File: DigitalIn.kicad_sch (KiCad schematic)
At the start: 5 parts, among them U7 LTV-247

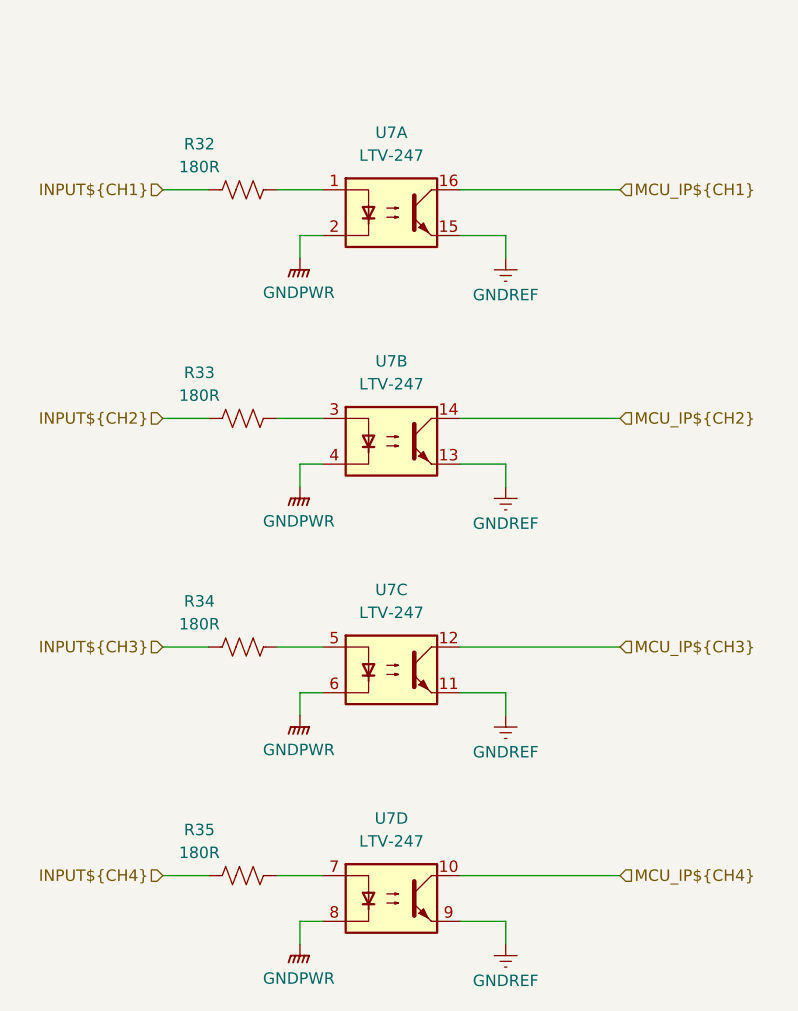
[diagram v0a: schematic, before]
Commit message: Changes to input after testing with some optical sensors
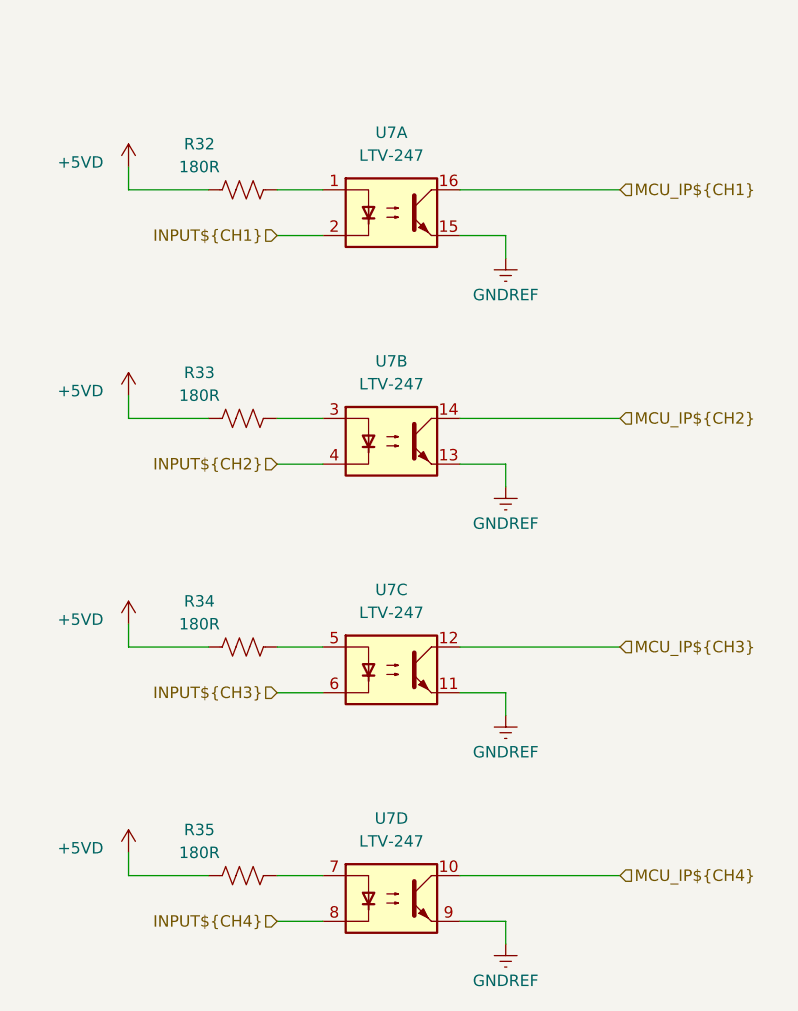
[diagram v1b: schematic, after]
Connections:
- net INPUT${CH1}: now also U7.2; no longer R32.1
- net INPUT${CH2}: now also U7.4; no longer R33.1
- net INPUT${CH3}: now also U7.6; no longer R34.1
- net INPUT${CH4}: now also U7.8; no longer R35.1
- removed net GNDPWR: U7.2, U7.4, U7.6, U7.8
- new net +5VD: R32.1, R33.1, R34.1, R35.1

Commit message: Added high speed encoder input circuitry. General tidy and updates to readme
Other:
- note added: "NPN Inputs"
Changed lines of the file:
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@@
 	(generator_version "9.0")
 	(paper "A4")
+	(text "NPN Inputs"
+		(exclude_from_sim no)
+		(at 149.606 35.814 0)
+		(effects
+			(font
+				(size 1.27 1.27)
+			)
+		)
+	)
 	(wire
 		(pts
@@
 			(project "Remora Nucleo F446ZE Hat"
 				(path "/5473abc6-7b93-43cc-a401-f691c4d7d7cf/181d5939-8311-41b3-8216-f7233e3a75eb/1fe6751c-d44f-4f1b-8c0c-fbb5540720e0"
-					(reference "#PWR0219")
+					(reference "#PWR0225")
 					(unit 1)
 				)
@@
 			(project ""
 				(path "/5473abc6-7b93-43cc-a401-f691c4d7d7cf/181d5939-8311-41b3-8216-f7233e3a75eb/1fe6751c-d44f-4f1b-8c0c-fbb5540720e0"
-					(reference "U20")
+					(reference "U16")
 					(unit 4)
 				)
@@
 			(project "Remora Nucleo F446ZE Hat"
 				(path "/5473abc6-7b93-43cc-a401-f691c4d7d7cf/181d5939-8311-41b3-8216-f7233e3a75eb/1fe6751c-d44f-4f1b-8c0c-fbb5540720e0"
-					(reference "#PWR0217")
+					(reference "#PWR0223")
 					(unit 1)
 				)
@@
 			(project "Remora Nucleo F446ZE Hat"
 				(path "/5473abc6-7b93-43cc-a401-f691c4d7d7cf/181d5939-8311-41b3-8216-f7233e3a75eb/1fe6751c-d44f-4f1b-8c0c-fbb5540720e0"
-					(reference "#PWR0214")
+					(reference "#PWR0220")
 					(unit 1)
 				)
@@
 			(project "Remora Nucleo F446ZE Hat"
 				(path "/5473abc6-7b93-43cc-a401-f691c4d7d7cf/181d5939-8311-41b3-8216-f7233e3a75eb/1fe6751c-d44f-4f1b-8c0c-fbb5540720e0"
-					(reference "R88")
+					(reference "R95")
 					(unit 1)
 				)
@@
 			(project ""
 				(path "/5473abc6-7b93-43cc-a401-f691c4d7d7cf/181d5939-8311-41b3-8216-f7233e3a75eb/1fe6751c-d44f-4f1b-8c0c-fbb5540720e0"
-					(reference "U20")
+					(reference "U17")
 					(unit 2)
 				)
@@
 			(project ""
 				(path "/5473abc6-7b93-43cc-a401-f691c4d7d7cf/181d5939-8311-41b3-8216-f7233e3a75eb/1fe6751c-d44f-4f1b-8c0c-fbb5540720e0"
-					(reference "U20")
+					(reference "U17")
 					(unit 3)
 				)
@@
 			(project "Remora Nucleo F446ZE Hat"
 				(path "/5473abc6-7b93-43cc-a401-f691c4d7d7cf/181d5939-8311-41b3-8216-f7233e3a75eb/1fe6751c-d44f-4f1b-8c0c-fbb5540720e0"
-					(reference "#PWR0218")
+					(reference "#PWR0224")
 					(unit 1)
 				)
@@
 			(project "Remora Nucleo F446ZE Hat"
 				(path "/5473abc6-7b93-43cc-a401-f691c4d7d7cf/181d5939-8311-41b3-8216-f7233e3a75eb/1fe6751c-d44f-4f1b-8c0c-fbb5540720e0"
-					(reference "R89")
+					(reference "R96")
 					(unit 1)
 				)
@@
 			(project "Remora Nucleo F446ZE Hat"
 				(path "/5473abc6-7b93-43cc-a401-f691c4d7d7cf/181d5939-8311-41b3-8216-f7233e3a75eb/1fe6751c-d44f-4f1b-8c0c-fbb5540720e0"
-					(reference "#PWR0216")
+					(reference "#PWR0222")
 					(unit 1)
 				)
@@
 			(project "Remora Nucleo F446ZE Hat"
 				(path "/5473abc6-7b93-43cc-a401-f691c4d7d7cf/181d5939-8311-41b3-8216-f7233e3a75eb/1fe6751c-d44f-4f1b-8c0c-fbb5540720e0"
-					(reference "#PWR0221")
+					(reference "#PWR0227")
 					(unit 1)
 				)
@@
 			(project ""
 				(path "/5473abc6-7b93-43cc-a401-f691c4d7d7cf/181d5939-8311-41b3-8216-f7233e3a75eb/1fe6751c-d44f-4f1b-8c0c-fbb5540720e0"
-					(reference "U20")
+					(reference "U19")
 					(unit 1)
 				)
@@
 			(project "Remora Nucleo F446ZE Hat"
 				(path "/5473abc6-7b93-43cc-a401-f691c4d7d7cf/181d5939-8311-41b3-8216-f7233e3a75eb/1fe6751c-d44f-4f1b-8c0c-fbb5540720e0"
-					(reference "#PWR0215")
+					(reference "#PWR0221")
 					(unit 1)
 				)
@@
 			(project "Remora Nucleo F446ZE Hat"
 				(path "/5473abc6-7b93-43cc-a401-f691c4d7d7cf/181d5939-8311-41b3-8216-f7233e3a75eb/1fe6751c-d44f-4f1b-8c0c-fbb5540720e0"
-					(reference "#PWR0220")
+					(reference "#PWR0226")
 					(unit 1)
 				)
@@
 			(project "Remora Nucleo F446ZE Hat"
 				(path "/5473abc6-7b93-43cc-a401-f691c4d7d7cf/181d5939-8311-41b3-8216-f7233e3a75eb/1fe6751c-d44f-4f1b-8c0c-fbb5540720e0"
-					(reference "R90")
+					(reference "R97")
 					(unit 1)
 				)
@@
 			(project "Remora Nucleo F446ZE Hat"
 				(path "/5473abc6-7b93-43cc-a401-f691c4d7d7cf/181d5939-8311-41b3-8216-f7233e3a75eb/1fe6751c-d44f-4f1b-8c0c-fbb5540720e0"
-					(reference "R91")
-					(unit 1)
-				)
+					(reference "R98")
+					(unit 1)
+				)

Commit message: Layout for stepper drivers and digital inputs
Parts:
- renumbered U7 to U
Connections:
- net GNDREF: now also U.15, U.15, U.15; no longer U.11, U.13, U.9
- net INPUT${CH2}: now also U.2; no longer U.4
- net INPUT${CH3}: now also U.2; no longer U.6
- net INPUT${CH4}: now also U.2; no longer U.8
- net MCU_IP${CH2}: now also U.16; no longer U.14
- net MCU_IP${CH3}: now also U.16; no longer U.12
- net MCU_IP${CH4}: now also U.16; no longer U.10
- net at R35.2: now also U.1; no longer U.7
- net at R33.2: now also U.1; no longer U.3
- net at R34.2: now also U.1; no longer U.5
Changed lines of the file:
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@@
 		(instances
 			(project "Remora Nucleo F446ZE Hat"
-				(path "/5473abc6-7b93-43cc-a401-f691c4d7d7cf/181d5939-8311-41b3-8216-f7233e3a75eb/1fe6751c-d44f-4f1b-8c0c-fbb5540720e0"
-					(reference "#PWR0225")
+				(path "/5473abc6-7b93-43cc-a401-f691c4d7d7cf/181d5939-8311-41b3-8216-f7233e3a75eb/0efd5135-f8b7-4cd1-8e93-f14156388778"
+					(reference "#PWR0228")
 					(unit 1)
 				)
@@
 		(lib_id "Isolator:LTV-247")
 		(at 149.86 132.08 0)
-		(unit 4)
+		(unit 1)
 		(exclude_from_sim no)
 		(in_bom yes)
@@
 		(dnp no)
 		(fields_autoplaced yes)
-		(property "Reference" "U7"
+		(property "Reference" "U"
 			(at 149.86 123.19 0)
 			(effects
@@
 		)
 		(instances
-			(project ""
-				(path "/5473abc6-7b93-43cc-a401-f691c4d7d7cf/181d5939-8311-41b3-8216-f7233e3a75eb/1fe6751c-d44f-4f1b-8c0c-fbb5540720e0"
+			(project "Remora Nucleo F446ZE Hat"
+				(path "/5473abc6-7b93-43cc-a401-f691c4d7d7cf/181d5939-8311-41b3-8216-f7233e3a75eb/0efd5135-f8b7-4cd1-8e93-f14156388778"
 					(reference "U16")
 					(unit 4)
 				)
-				(path "/5473abc6-7b93-43cc-a401-f691c4d7d7cf/181d5939-8311-41b3-8216-f7233e3a75eb/38a9b34d-220a-4331-8671-09e3a6b76818"
-					(reference "U10")
-					(unit 4)
-				)
-				(path "/5473abc6-7b93-43cc-a401-f691c4d7d7cf/181d5939-8311-41b3-8216-f7233e3a75eb/3ddea5d6-e83a-4299-ab19-77514b1abca5"
-					(reference "U9")
-					(unit 4)
-				)
-				(path "/5473abc6-7b93-43cc-a401-f691c4d7d7cf/181d5939-8311-41b3-8216-f7233e3a75eb/adf08f85-0659-4d18-9c0c-1da5c9849bec"
-					(reference "U7")
-					(unit 4)
-				)
 			)
 		)
@@
 		(instances
 			(project "Remora Nucleo F446ZE Hat"
-				(path "/5473abc6-7b93-43cc-a401-f691c4d7d7cf/181d5939-8311-41b3-8216-f7233e3a75eb/1fe6751c-d44f-4f1b-8c0c-fbb5540720e0"
-					(reference "#PWR0223")
+				(path "/5473abc6-7b93-43cc-a401-f691c4d7d7cf/181d5939-8311-41b3-8216-f7233e3a75eb/0efd5135-f8b7-4cd1-8e93-f14156388778"
+					(reference "#PWR0226")
 					(unit 1)
 				)
@@
 		(instances
 			(project "Remora Nucleo F446ZE Hat"
-				(path "/5473abc6-7b93-43cc-a401-f691c4d7d7cf/181d5939-8311-41b3-8216-f7233e3a75eb/1fe6751c-d44f-4f1b-8c0c-fbb5540720e0"
-					(reference "#PWR0220")
+				(path "/5473abc6-7b93-43cc-a401-f691c4d7d7cf/181d5939-8311-41b3-8216-f7233e3a75eb/0efd5135-f8b7-4cd1-8e93-f14156388778"
+					(reference "#PWR0223")
 					(unit 1)
 				)
@@
 		(instances
 			(project "Remora Nucleo F446ZE Hat"
-				(path "/5473abc6-7b93-43cc-a401-f691c4d7d7cf/181d5939-8311-41b3-8216-f7233e3a75eb/1fe6751c-d44f-4f1b-8c0c-fbb5540720e0"
+				(path "/5473abc6-7b93-43cc-a401-f691c4d7d7cf/181d5939-8311-41b3-8216-f7233e3a75eb/0efd5135-f8b7-4cd1-8e93-f14156388778"
 					(reference "R95")
 					(unit 1)
@@
 		(lib_id "Isolator:LTV-247")
 		(at 149.86 81.28 0)
-		(unit 2)
+		(unit 1)
 		(exclude_from_sim no)
 		(in_bom yes)
@@
 		(dnp no)
 		(fields_autoplaced yes)
-		(property "Reference" "U7"
+		(property "Reference" "U"
 			(at 149.86 72.39 0)
 			(effects
@@
 		)
 		(instances
-			(project ""
-				(path "/5473abc6-7b93-43cc-a401-f691c4d7d7cf/181d5939-8311-41b3-8216-f7233e3a75eb/1fe6751c-d44f-4f1b-8c0c-fbb5540720e0"
+			(project "Remora Nucleo F446ZE Hat"
+				(path "/5473abc6-7b93-43cc-a401-f691c4d7d7cf/181d5939-8311-41b3-8216-f7233e3a75eb/0efd5135-f8b7-4cd1-8e93-f14156388778"
 					(reference "U17")
 					(unit 2)
 				)
-				(path "/5473abc6-7b93-43cc-a401-f691c4d7d7cf/181d5939-8311-41b3-8216-f7233e3a75eb/38a9b34d-220a-4331-8671-09e3a6b76818"
-					(reference "U10")
-					(unit 2)
-				)
-				(path "/5473abc6-7b93-43cc-a401-f691c4d7d7cf/181d5939-8311-41b3-8216-f7233e3a75eb/3ddea5d6-e83a-4299-ab19-77514b1abca5"
-					(reference "U9")
-					(unit 2)
-				)
-				(path "/5473abc6-7b93-43cc-a401-f691c4d7d7cf/181d5939-8311-41b3-8216-f7233e3a75eb/adf08f85-0659-4d18-9c0c-1da5c9849bec"
-					(reference "U7")
-					(unit 2)
-				)
 			)
 		)
@@
 		(lib_id "Isolator:LTV-247")
 		(at 149.86 106.68 0)
-		(unit 3)
+		(unit 1)
 		(exclude_from_sim no)
 		(in_bom yes)
@@
 		(dnp no)
 		(fields_autoplaced yes)
-		(property "Reference" "U7"
+		(property "Reference" "U"
 			(at 149.86 97.79 0)
 			(effects
@@
 		)
 		(instances
-			(project ""
-				(path "/5473abc6-7b93-43cc-a401-f691c4d7d7cf/181d5939-8311-41b3-8216-f7233e3a75eb/1fe6751c-d44f-4f1b-8c0c-fbb5540720e0"
+			(project "Remora Nucleo F446ZE Hat"
+				(path "/5473abc6-7b93-43cc-a401-f691c4d7d7cf/181d5939-8311-41b3-8216-f7233e3a75eb/0efd5135-f8b7-4cd1-8e93-f14156388778"
 					(reference "U17")
 					(unit 3)
 				)
-				(path "/5473abc6-7b93-43cc-a401-f691c4d7d7cf/181d5939-8311-41b3-8216-f7233e3a75eb/38a9b34d-220a-4331-8671-09e3a6b76818"
-					(reference "U10")
-					(unit 3)
-				)
-				(path "/5473abc6-7b93-43cc-a401-f691c4d7d7cf/181d5939-8311-41b3-8216-f7233e3a75eb/3ddea5d6-e83a-4299-ab19-77514b1abca5"
-					(reference "U9")
-					(unit 3)
-				)
-				(path "/5473abc6-7b93-43cc-a401-f691c4d7d7cf/181d5939-8311-41b3-8216-f7233e3a75eb/adf08f85-0659-4d18-9c0c-1da5c9849bec"
-					(reference "U7")
-					(unit 3)
-				)
 			)
 		)
@@
 		(instances
 			(project "Remora Nucleo F446ZE Hat"
-				(path "/5473abc6-7b93-43cc-a401-f691c4d7d7cf/181d5939-8311-41b3-8216-f7233e3a75eb/1fe6751c-d44f-4f1b-8c0c-fbb5540720e0"
-					(reference "#PWR0224")
+				(path "/5473abc6-7b93-43cc-a401-f691c4d7d7cf/181d5939-8311-41b3-8216-f7233e3a75eb/0efd5135-f8b7-4cd1-8e93-f14156388778"
+					(reference "#PWR0227")
 					(unit 1)
 				)
@@
 		(instances
 			(project "Remora Nucleo F446ZE Hat"
-				(path "/5473abc6-7b93-43cc-a401-f691c4d7d7cf/181d5939-8311-41b3-8216-f7233e3a75eb/1fe6751c-d44f-4f1b-8c0c-fbb5540720e0"
+				(path "/5473abc6-7b93-43cc-a401-f691c4d7d7cf/181d5939-8311-41b3-8216-f7233e3a75eb/0efd5135-f8b7-4cd1-8e93-f14156388778"
 					(reference "R96")
 					(unit 1)
@@
 		(instances
 			(project "Remora Nucleo F446ZE Hat"
-				(path "/5473abc6-7b93-43cc-a401-f691c4d7d7cf/181d5939-8311-41b3-8216-f7233e3a75eb/1fe6751c-d44f-4f1b-8c0c-fbb5540720e0"
-					(reference "#PWR0222")
+				(path "/5473abc6-7b93-43cc-a401-f691c4d7d7cf/181d5939-8311-41b3-8216-f7233e3a75eb/0efd5135-f8b7-4cd1-8e93-f14156388778"
+					(reference "#PWR0225")
 					(unit 1)
 				)
@@
 		(instances
 			(project "Remora Nucleo F446ZE Hat"
-				(path "/5473abc6-7b93-43cc-a401-f691c4d7d7cf/181d5939-8311-41b3-8216-f7233e3a75eb/1fe6751c-d44f-4f1b-8c0c-fbb5540720e0"
-					(reference "#PWR0227")
+				(path "/5473abc6-7b93-43cc-a401-f691c4d7d7cf/181d5939-8311-41b3-8216-f7233e3a75eb/0efd5135-f8b7-4cd1-8e93-f14156388778"
+					(reference "#PWR0230")
 					(unit 1)
 				)
@@
 		(dnp no)
 		(fields_autoplaced yes)
-		(property "Reference" "U7"
+		(property "Reference" "U"
 			(at 149.86 46.99 0)
 			(effects
@@
 		)
 		(instances
-			(project ""
-				(path "/5473abc6-7b93-43cc-a401-f691c4d7d7cf/181d5939-8311-41b3-8216-f7233e3a75eb/1fe6751c-d44f-4f1b-8c0c-fbb5540720e0"
+			(project "Remora Nucleo F446ZE Hat"
+				(path "/5473abc6-7b93-43cc-a401-f691c4d7d7cf/181d5939-8311-41b3-8216-f7233e3a75eb/0efd5135-f8b7-4cd1-8e93-f14156388778"
 					(reference "U19")
-					(unit 1)
-				)
-				(path "/5473abc6-7b93-43cc-a401-f691c4d7d7cf/181d5939-8311-41b3-8216-f7233e3a75eb/38a9b34d-220a-4331-8671-09e3a6b76818"
-					(reference "U10")
-					(unit 1)
-				)
-				(path "/5473abc6-7b93-43cc-a401-f691c4d7d7cf/181d5939-8311-41b3-8216-f7233e3a75eb/3ddea5d6-e83a-4299-ab19-77514b1abca5"
-					(reference "U9")
-					(unit 1)
-				)
-				(path "/5473abc6-7b93-43cc-a401-f691c4d7d7cf/181d5939-8311-41b3-8216-f7233e3a75eb/adf08f85-0659-4d18-9c0c-1da5c9849bec"
-					(reference "U7")
 					(unit 1)
 				)
@@
 		(instances
 			(project "Remora Nucleo F446ZE Hat"
-				(path "/5473abc6-7b93-43cc-a401-f691c4d7d7cf/181d5939-8311-41b3-8216-f7233e3a75eb/1fe6751c-d44f-4f1b-8c0c-fbb5540720e0"
-					(reference "#PWR0221")
+				(path "/5473abc6-7b93-43cc-a401-f691c4d7d7cf/181d5939-8311-41b3-8216-f7233e3a75eb/0efd5135-f8b7-4cd1-8e93-f14156388778"
+					(reference "#PWR0224")
 					(unit 1)
 				)
@@
 		(instances
 			(project "Remora Nucleo F446ZE Hat"
-				(path "/5473abc6-7b93-43cc-a401-f691c4d7d7cf/181d5939-8311-41b3-8216-f7233e3a75eb/1fe6751c-d44f-4f1b-8c0c-fbb5540720e0"
-					(reference "#PWR0226")
+				(path "/5473abc6-7b93-43cc-a401-f691c4d7d7cf/181d5939-8311-41b3-8216-f7233e3a75eb/0efd5135-f8b7-4cd1-8e93-f14156388778"
+					(reference "#PWR0229")
 					(unit 1)
 				)
@@
 		(instances
 			(project "Remora Nucleo F446ZE Hat"
-				(path "/5473abc6-7b93-43cc-a401-f691c4d7d7cf/181d5939-8311-41b3-8216-f7233e3a75eb/1fe6751c-d44f-4f1b-8c0c-fbb5540720e0"
+				(path "/5473abc6-7b93-43cc-a401-f691c4d7d7cf/181d5939-8311-41b3-8216-f7233e3a75eb/0efd5135-f8b7-4cd1-8e93-f14156388778"
 					(reference "R97")
 					(unit 1)
@@
 		(instances
 			(project "Remora Nucleo F446ZE Hat"
-				(path "/5473abc6-7b93-43cc-a401-f691c4d7d7cf/181d5939-8311-41b3-8216-f7233e3a75eb/1fe6751c-d44f-4f1b-8c0c-fbb5540720e0"
+				(path "/5473abc6-7b93-43cc-a401-f691c4d7d7cf/181d5939-8311-41b3-8216-f7233e3a75eb/0efd5135-f8b7-4cd1-8e93-f14156388778"
 					(reference "R98")
 					(unit 1)

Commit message: Switched terminal footprints over to a finer pitch. Corrected an issue with component reference values preventing proper use of multi channel rule areas. Component references for 4 channel optos are more straightforward as a result
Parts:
- removed U (x4): LTV-247, Package_SO:SOP-16_4.4x10.4mm_P1.27mm, symbol Isolator:LTV-247
- added U7: LTV-247, Package_SO:SOP-16_4.4x10.4mm_P1.27mm, symbol Isolator:LTV-247
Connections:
- net GNDREF: now also U7.11, U7.13, U7.15, U7.9
- net INPUT${CH1}: now also U7.2
- net INPUT${CH2}: now also U7.4
- net INPUT${CH3}: now also U7.6
- net INPUT${CH4}: now also U7.8
- net MCU_IP${CH1}: now also U7.16
- net MCU_IP${CH2}: now also U7.14
- net MCU_IP${CH3}: now also U7.12
- net MCU_IP${CH4}: now also U7.10
- net at R35.2: now also U7.7
- net at R32.2: now also U7.1
- net at R33.2: now also U7.3
- net at R34.2: now also U7.5

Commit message: Caught some errors with spacing of jumpers, did some BOM consolidation and included BOM. Updates to Gerbers to reflect new changes.
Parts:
- U7: Digikey Part Number (none) -> 160-2255-1-ND
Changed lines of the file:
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@@
+			)
+		)
+		(property "Digikey Part Number" "160-2255-1-ND"
+			(at 149.86 132.08 0)
+			(effects
+				(font
+					(size 1.27 1.27)
+				)
 			)
 		)
@@
 			)
 		)
+		(property "Digikey Part Number" "160-2255-1-ND"
+			(at 149.86 106.68 0)
+			(effects
+				(font
+					(size 1.27 1.27)
+				)
+			)
+		)
 		(pin "15"
 		)
@@
 			)
 		)
+		(property "Digikey Part Number" "160-2255-1-ND"
+			(at 149.86 81.28 0)
+			(effects
+				(font
+					(size 1.27 1.27)
+				)
+			)
+		)
 		(pin "15"
 		)
@@
 			)
 		)
+		(property "Digikey Part Number" "160-2255-1-ND"
+			(at 149.86 55.88 0)
+			(effects
+				(font
+					(size 1.27 1.27)
+				)
+			)
+		)
